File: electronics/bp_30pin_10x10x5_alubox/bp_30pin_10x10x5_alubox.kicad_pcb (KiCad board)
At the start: 2 copper layers, 80 x 40 mm, 2 parts

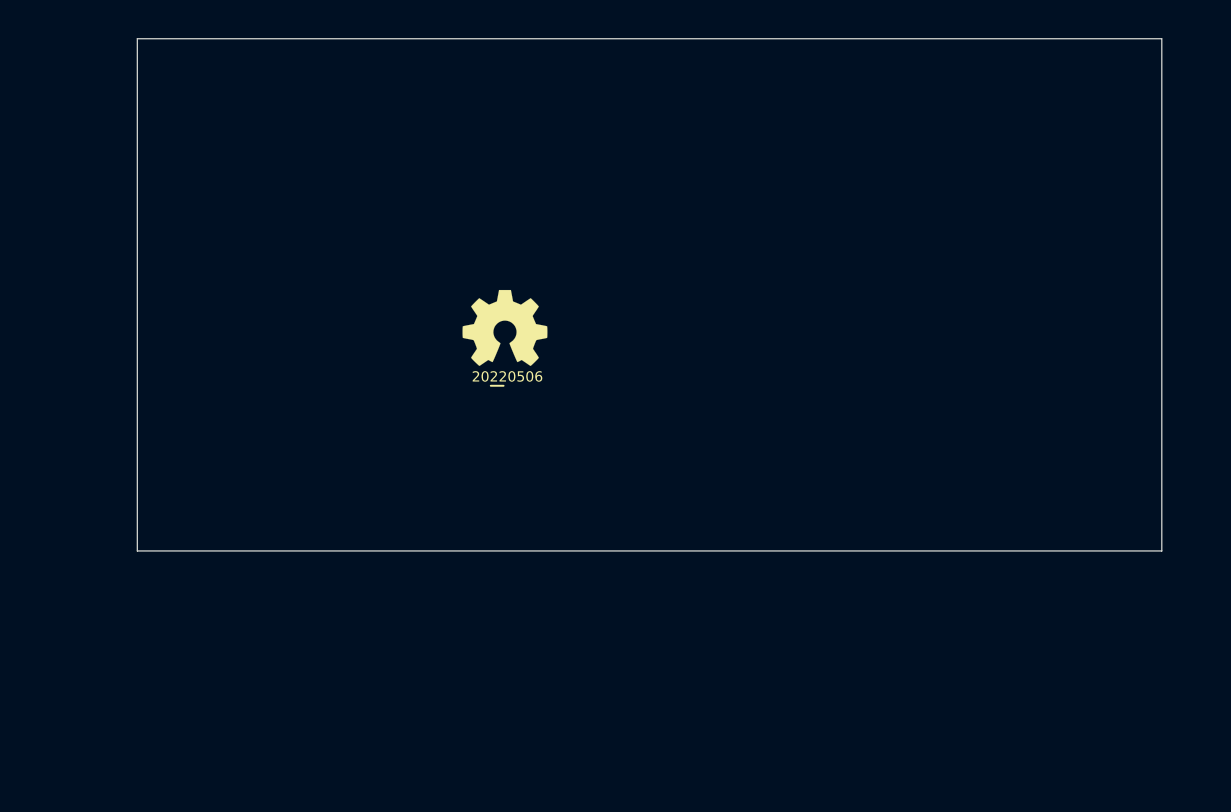
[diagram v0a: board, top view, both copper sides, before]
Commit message: added lock files to gitignore, WIP 30 pin backplane
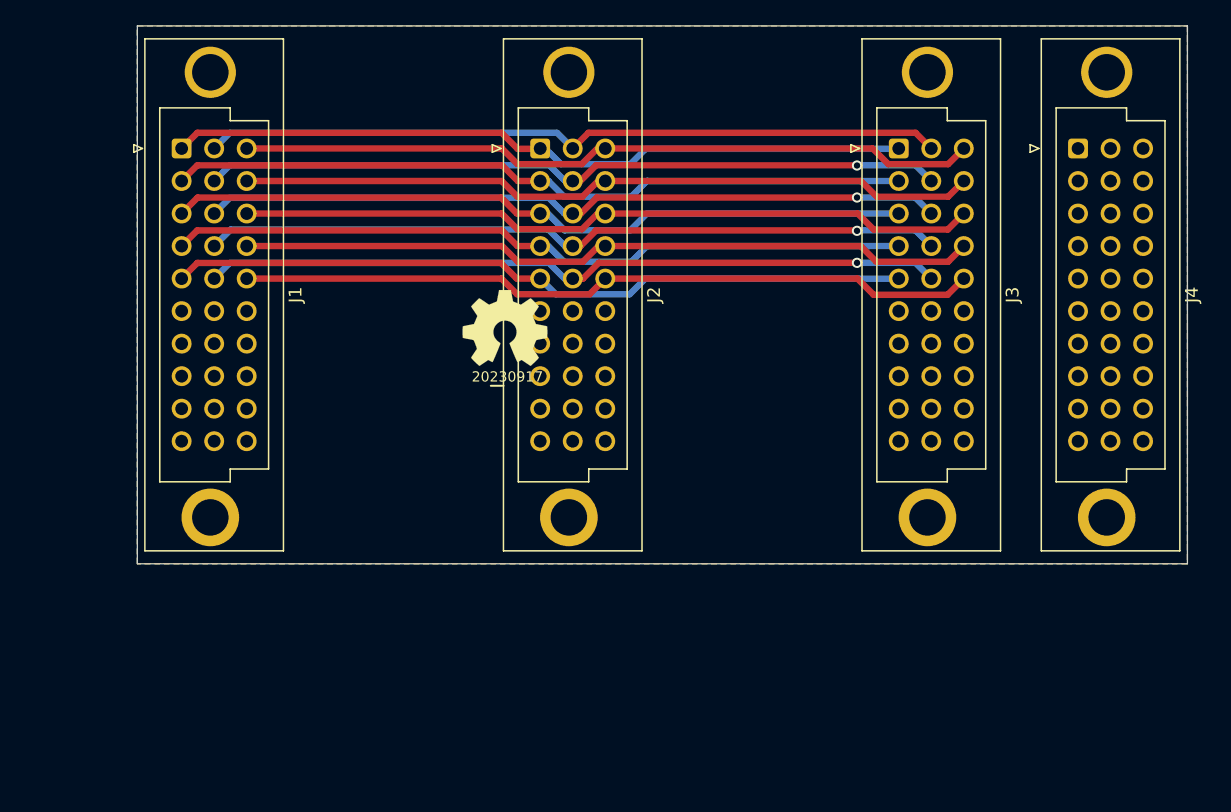
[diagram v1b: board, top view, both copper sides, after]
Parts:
- added J1: ~, SquantorConnectors:DIN41612_C3_3x10_Female_Vertical_THT_shields, F.Cu at (116.0, 85.0)
- added J2: ~, SquantorConnectors:DIN41612_C3_3x10_Female_Vertical_THT_shields, F.Cu at (144.0, 85.0)
- added J3: ~, SquantorConnectors:DIN41612_C3_3x10_Female_Vertical_THT_shields, F.Cu at (172.0, 85.0)
- added J4: ~, SquantorConnectors:DIN41612_C3_3x10_Female_Vertical_THT_shields, F.Cu at (186.0, 85.0)
- N1: value 20220506 -> 20230917
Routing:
- net /A3: track 0.00 -> 58.1 mm
- net /B4: track 0.00 -> 58.1 mm, vias 0 -> 1
- net /C5: track 0.00 -> 58.1 mm
- net /A5: track 0.00 -> 58.1 mm
- net /A1: track 0.00 -> 58.1 mm
- net /B3: track 0.00 -> 58.1 mm, vias 0 -> 1
- net /C3: track 0.00 -> 58.1 mm
- net /B2: track 0.00 -> 58.0 mm, vias 0 -> 1
- net /A2: track 0.00 -> 58.0 mm
- net /B5: track 0.00 -> 58.0 mm, vias 0 -> 1
- net /C4: track 0.00 -> 58.0 mm
- net /C1: track 0.00 -> 58.0 mm
- net /A4: track 0.00 -> 58.0 mm
- net /B1: track 0.00 -> 58.0 mm
- net /C2: track 0.00 -> 58.0 mm
- added copper zone on B.Cu, net Earth
- added copper zone on F.Cu, net Earth
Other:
- board size 80 x 40 mm -> 82 x 42 mm

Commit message: Place and route done
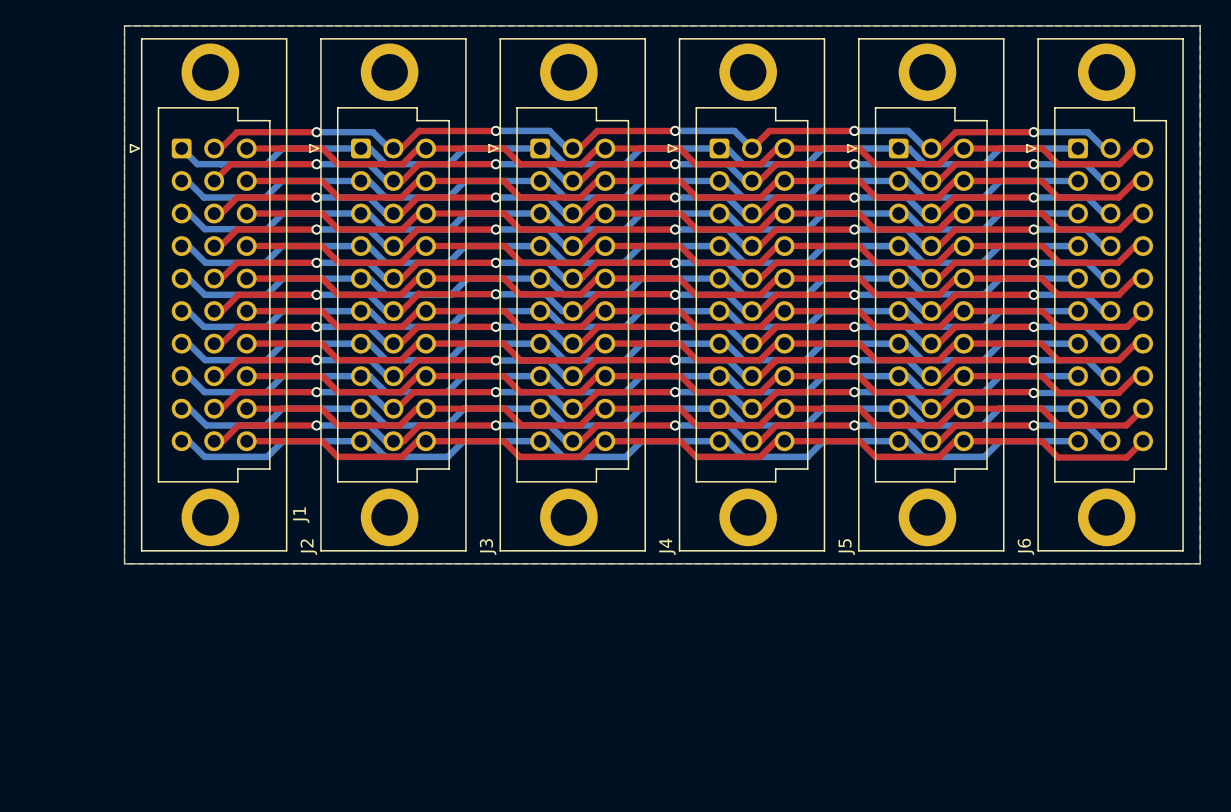
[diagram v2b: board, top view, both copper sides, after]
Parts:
- added J5: ~, SquantorConnectors:DIN41612_R3_3x10_Male_Vertical_THT_shield, F.Cu at (172.0, 85.0)
- added J6: ~, SquantorConnectors:DIN41612_R3_3x10_Male_Vertical_THT_shield, F.Cu at (186.0, 85.0)
- J1, J2, J3, J4: footprint SquantorConnectors:DIN41612_C3_3x10_Female_Vertical_THT_shields -> SquantorConnectors:DIN41612_R3_3x10_Male_Vertical_THT_shield
- N1, N2: moved to B.Cu
- moved J3 28.0 mm to (144.0, 85.0)
- moved J4 28.0 mm to (158.0, 85.0)
- moved N2 19.9 mm to (123.1, 100.0), turned to 180 degrees
- moved N1 19.0 mm to (123.7, 103.9), turned to 180 degrees
- moved J2 14.0 mm to (130.0, 85.0)
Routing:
- net /B7: track 0.00 -> 75.4 mm, vias 0 -> 5
- net /A9: track 0.00 -> 75.4 mm
- net /C9: track 0.00 -> 75.4 mm
- net /C7: track 0.00 -> 75.4 mm
- net /B6: track 0.00 -> 75.4 mm, vias 0 -> 5
- net /B9: track 0.00 -> 75.3 mm, vias 0 -> 5
- net /A7: track 0.00 -> 75.3 mm
- net /C8: track 0.00 -> 75.2 mm
- net /A8: track 0.00 -> 75.2 mm
- net /B8: track 0.00 -> 75.2 mm, vias 0 -> 5
- net /C10: track 0.00 -> 75.1 mm
- net /B10: track 0.00 -> 75.1 mm, vias 0 -> 5
- net /A6: track 0.00 -> 75.1 mm
- net /C6: track 0.00 -> 75.1 mm
- net /A10: track 0.00 -> 75.1 mm
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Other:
- board size 82 x 42 mm -> 84 x 42 mm

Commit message: updated versionnumber, added block for backplane, larger copper plane spacing
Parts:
- N1: value 20230917 -> 20231204
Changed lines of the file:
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@@
         (effects (font (size 1 1) (thickness 0.15)) (justify mirror))
     )
-    (fp_text value "20230917" (at 0.8 0.1) (layer "B.SilkS")
+    (fp_text value "20231204" (at 0.8 0.1) (layer "B.SilkS")
         (effects (font (size 0.8 0.8) (thickness 0.15)) (justify mirror))
     )
@@
   (gr_line (start 109 64) (end 109 106)
     (stroke (width 0.05) (type default)) (layer "Edge.Cuts"))
-  (dimension (type aligned) (layer "Edge.Cuts")
+  (dimension (type aligned) (layer "Dwgs.User")
     (pts (xy 193 106) (xy 193 64))
     (height 4)
-    (gr_text "42,0000 mm" (at 198 85 90) (layer "Edge.Cuts")
+    (gr_text "42,0000 mm" (at 198 85 90) (layer "Dwgs.User")
       (effects (font (size 1 1) (thickness 0.15)))
     )
@@
     (style (thickness 0.05) (arrow_length 1.27) (text_position_mode 2) (extension_height 0.58642) (extension_offset 0.5) keep_text_aligned)
   )
-  (dimension (type aligned) (layer "Edge.Cuts")
+  (dimension (type aligned) (layer "Dwgs.User")
     (pts (xy 193 64) (xy 109 64))
     (height 4)
-    (gr_text "84,0000 mm" (at 151 59) (layer "Edge.Cuts")
+    (gr_text "84,0000 mm" (at 151 59) (layer "Dwgs.User")
       (effects (font (size 1 1) (thickness 0.15)))
     )
@@
   (segment (start 166.43 96.43) (end 160.54 96.43) (width 0.5) (layer "F.Cu") (net 30))
   (zone (net 31) (net_name "Earth") (layers "F&B.Cu") (hatch edge 0.5)
-    (connect_pads (clearance 0.3))
+    (connect_pads (clearance 0.5))
     (min_thickness 0.3) (filled_areas_thickness no)
     (fill yes (thermal_gap 0.3) (thermal_bridge_width 0.4))

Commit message: updated board to Aisler Budget design rules, fixed DRC errors
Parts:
- N1: value 20231204 -> 20231208

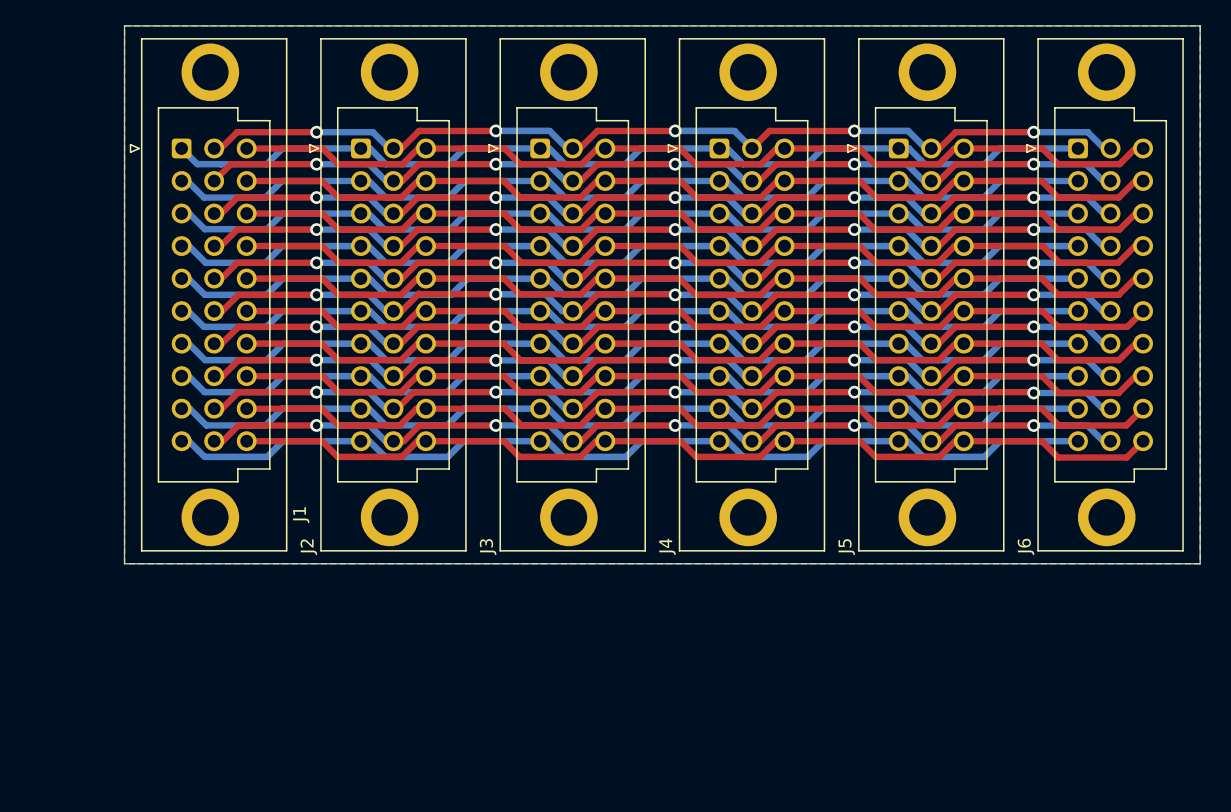
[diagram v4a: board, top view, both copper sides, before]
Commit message: removed one connector to give a 16mm pitch for the modules, one module will be a bit small cramped
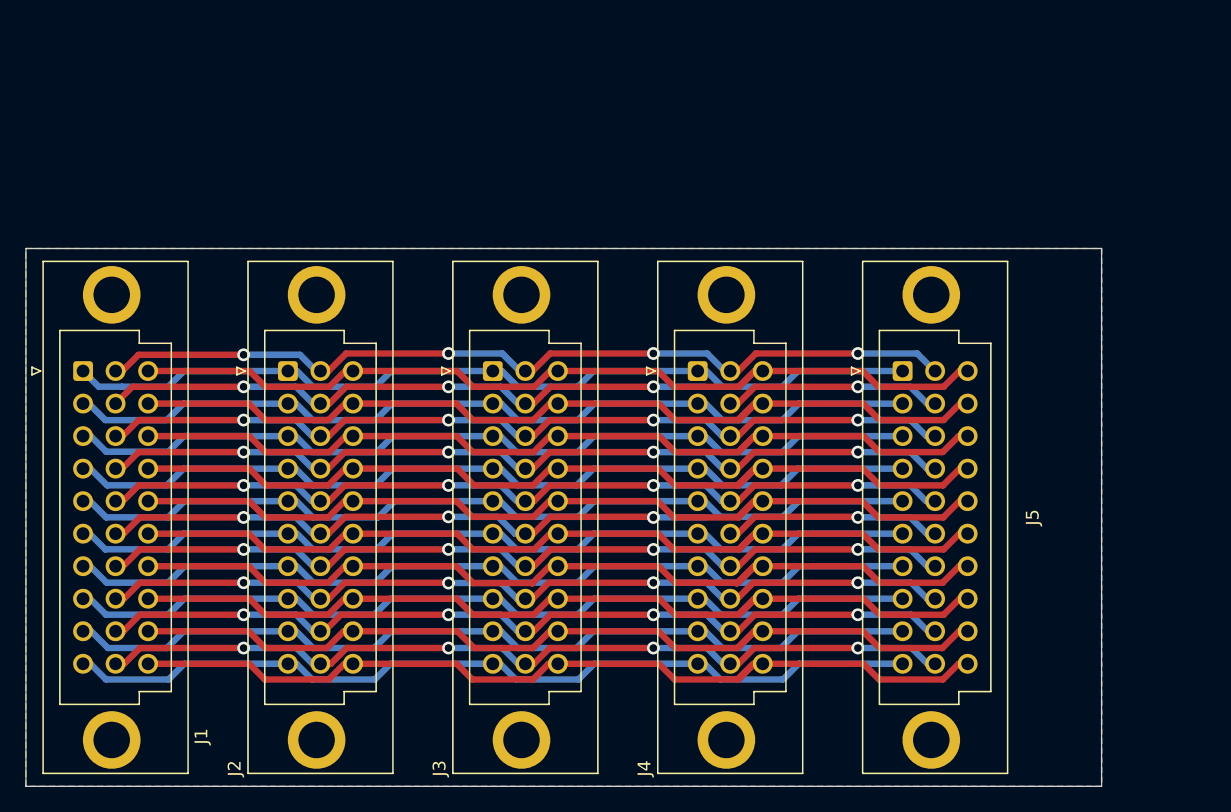
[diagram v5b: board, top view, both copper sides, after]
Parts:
- removed J6: ~, SquantorConnectors:DIN41612_R3_3x10_Male_Vertical_THT_shield
- moved J1 19.0 mm to (108.3, 102.4)
- moved N1 18.7 mm to (117.0, 121.4)
- moved N2 18.7 mm to (116.3, 117.4)
- moved J2 18.3 mm to (124.3, 102.4)
- moved J3 17.8 mm to (140.3, 102.4)
- moved J4 17.5 mm to (156.3, 102.4)
- moved J5 17.4 mm to (172.3, 102.4)
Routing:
- net /B2: track 75.4 -> 65.9 mm, vias 5 -> 4
- net /B6: track 75.4 -> 65.9 mm, vias 5 -> 4
- net /A9: track 75.4 -> 68.3 mm
- net /A4: track 75.4 -> 68.3 mm
- net /B7: track 75.4 -> 68.3 mm, vias 5 -> 4
- net /B4: track 75.4 -> 68.3 mm, vias 5 -> 4
- net /B9: track 75.3 -> 68.3 mm, vias 5 -> 4
- net /A2: track 75.3 -> 68.3 mm
- net /A7: track 75.3 -> 68.3 mm
- net /A1: track 75.1 -> 68.1 mm
- net /A5: track 75.2 -> 68.1 mm
- net /A8: track 75.2 -> 68.1 mm
- net /A3: track 75.2 -> 68.1 mm
- net /B8: track 75.2 -> 68.1 mm, vias 5 -> 4
- net /B3: track 75.2 -> 68.1 mm, vias 5 -> 4
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
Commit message: updated backplane to new components
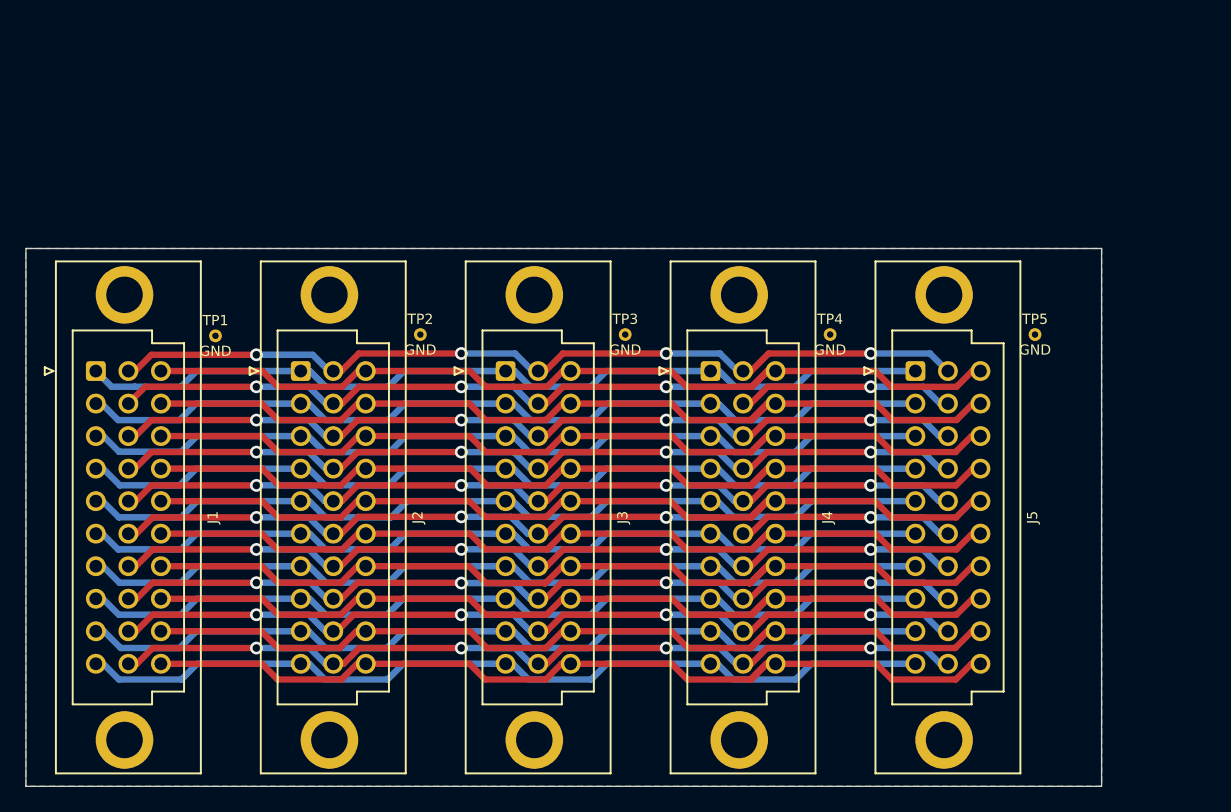
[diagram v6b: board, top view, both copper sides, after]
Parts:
- added TP1: GND, SquantorTestPoints:TestPoint_hole_H05R10, F.Cu at (116.1, 88.2)
- added TP2: GND, SquantorTestPoints:TestPoint_hole_H05R10, F.Cu at (132.1, 88.1)
- added TP3: GND, SquantorTestPoints:TestPoint_hole_H05R10, F.Cu at (148.1, 88.1)
- added TP4: GND, SquantorTestPoints:TestPoint_hole_H05R10, F.Cu at (164.1, 88.1)
- added TP5: GND, SquantorTestPoints:TestPoint_hole_H05R10, F.Cu at (180.1, 88.1)
- N1: value 20231208 -> 20240111
- moved J1 1.00 mm to (109.3, 102.4)
- moved J2 1.00 mm to (125.3, 102.4)
- moved J3 1.00 mm to (141.3, 102.4)
- moved J4 1.00 mm to (157.3, 102.4)
- moved J5 1.00 mm to (173.3, 102.4)
- moved N2 1.00 mm to (117.3, 117.4)

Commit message: prepared for production
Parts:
- N1: value 20240111 -> 20240216
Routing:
- net /C4: track 70.8 -> 68.1 mm
- net /C7: track 70.9 -> 68.3 mm
- net /C10: track 70.5 -> 68.1 mm
- net /B2: track 65.9 -> 68.3 mm
- net /C2: track 70.7 -> 68.3 mm
- net /C5: track 70.6 -> 68.3 mm
- net /C1: track 70.4 -> 68.2 mm
- net /B6: track 65.9 -> 68.2 mm
- net /C6: track 70.4 -> 68.1 mm

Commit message: prepared for production
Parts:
- N1: value 20240216 -> 20240218
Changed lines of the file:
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@@
         (effects (font (size 1 1) (thickness 0.15)) (justify mirror))
     )
-    (fp_text value "20240216" (at 0.8 0.1) (layer "B.SilkS")
+    (fp_text value "20240218" (at 0.8 0.1) (layer "B.SilkS")
         (effects (font (size 0.8 0.8) (thickness 0.15)) (justify mirror))
     )
